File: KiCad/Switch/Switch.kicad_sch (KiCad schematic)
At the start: 48 parts, among them Q1 BD139, Q2 IXTH90P10P, Q4 BD139, Q5A1 BSC340N08NS3G, Q6 BD139, U1 AD8033

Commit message: Simulation und PCB update
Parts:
- added V24: Conn_01x01, Connector:Banana_Jack_1Pin, symbol Connector_Generic:Conn_01x01
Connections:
- net 56V: no longer U1.7 (V+)
- new net: U1.7 (V+), V24.1 (Pin_1)

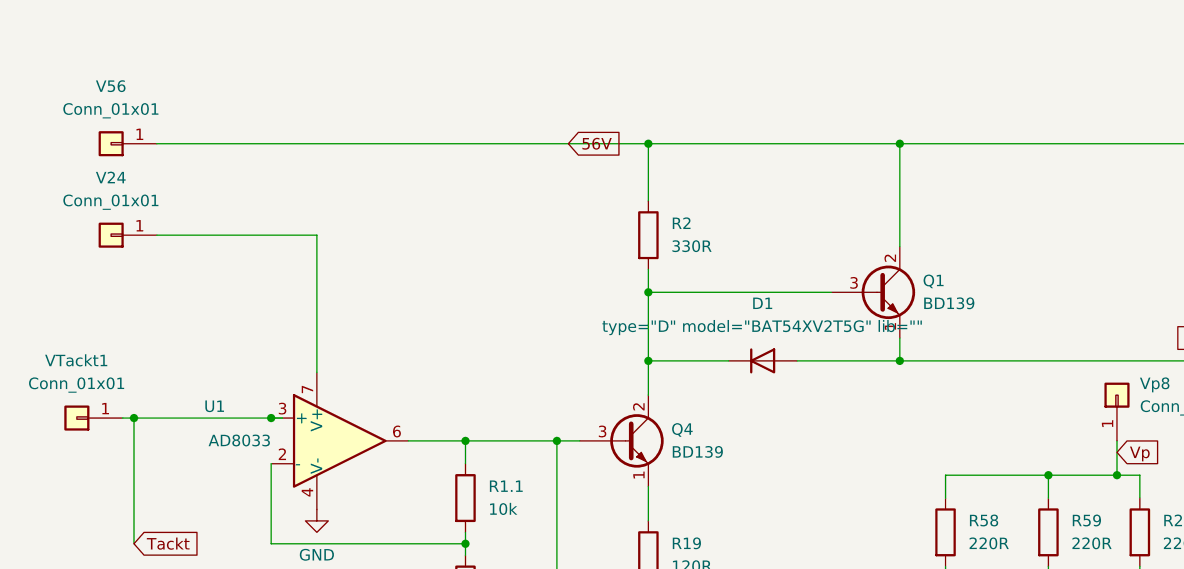
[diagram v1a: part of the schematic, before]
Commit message: kicad switch LDO install
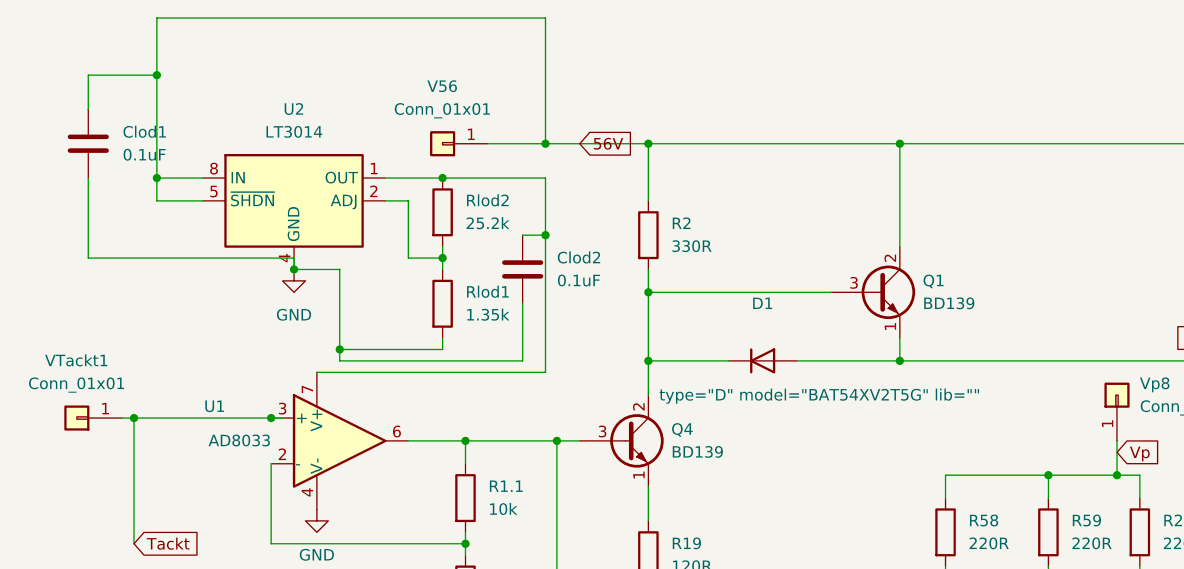
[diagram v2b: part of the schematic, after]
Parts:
- removed V24: Conn_01x01, Connector:Banana_Jack_1Pin, symbol Connector_Generic:Conn_01x01
- added Clod1, Clod2: 0.1uF, Capacitor_SMD:C_0805_2012Metric, symbol Device:C
- added Rlod1: 1.35k, Resistor_SMD:R_0805_2012Metric, symbol Device:R
- added Rlod2: 25.2k, Resistor_SMD:R_0805_2012Metric, symbol Device:R
- added U2: LT3014, Package_TO_SOT_SMD:SOT-23-5, symbol Regulator_Linear:LT3010
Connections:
- net 56V: now also Clod1.1, U2.5 (~{SHDN}), U2.8 (IN)
- net GND: now also Clod1.2, Clod2.2, Rlod1.2, U2.4 (GND), U2.9 (GND)
- net at U1.7 (V+): now also Clod2.1, Rlod2.1, U2.1 (OUT)
- new net: Rlod1.1, Rlod2.2, U2.2 (ADJ)
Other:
- moved on the sheet: V56
